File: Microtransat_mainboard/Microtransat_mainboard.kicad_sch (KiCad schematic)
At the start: 21 parts, among them J101 12V IN, J102 Conn_01x02, J103 Conn_01x06, J104 Conn_01x04, J105 Conn_01x04, J106 Conn_01x04, J107 Conn_01x04, SW101 SW_SPDT, U101 SD Card Module 254, U102 GPS 746, U103 IMU 4754

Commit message: Used correct battery voltage ~20V
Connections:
- net +12V renamed +20V
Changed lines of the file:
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@@
 			)
 		)
-		(property "Value" "+12V"
+		(property "Value" "+20V"
 			(at 29.21 52.07 0)
 			(effects
@@
 			)
 		)
-		(property "Value" "+12V"
+		(property "Value" "+20V"
 			(at 93.98 83.82 0)
 			(effects

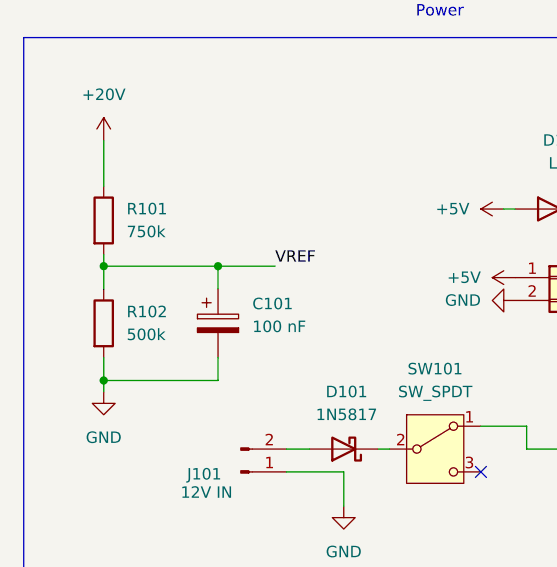
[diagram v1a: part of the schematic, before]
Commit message: Fixed voltage divider/high power voltage
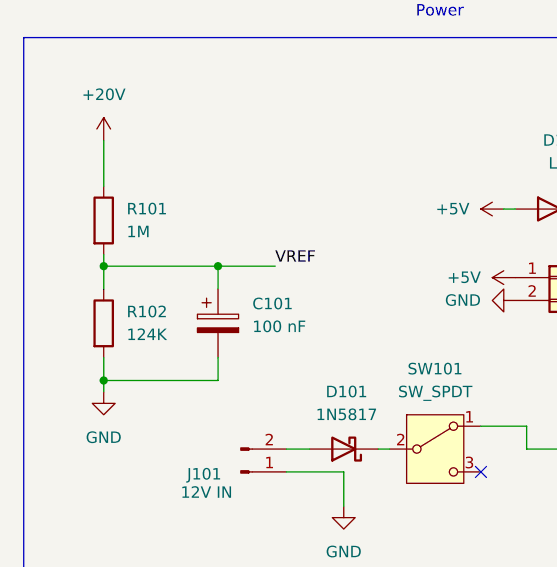
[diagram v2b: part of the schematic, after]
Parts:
- R101: value 750k -> 1M
- R102: value 500k -> 124K
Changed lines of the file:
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@@
 			)
 		)
-		(property "Value" "500k"
+		(property "Value" "124K"
 			(at 31.75 78.7399 0)
 			(effects
@@
 			)
 		)
-		(property "Value" "750k"
+		(property "Value" "1M"
 			(at 31.75 67.3099 0)
 			(effects
